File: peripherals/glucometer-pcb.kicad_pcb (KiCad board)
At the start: 2 copper layers, 36.5 x 59.9 mm, 19 parts, among them IC1 RC4558IP, IC2 LM1458N, IC3 RC4558IP

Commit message: change name
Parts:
- removed REF** (x2): MountingHole_2.2mm_M2_ISO7380, MountingHole:MountingHole_2.2mm_M2_ISO7380
- removed TP3: SIGNAL_OUT, TestPoint:TestPoint_Keystone_5015_Micro-Minature
- added BZ1: Buzzer, Buzzer_Beeper:MagneticBuzzer_Kingstate_KCG0601, F.Cu at (120.0, 106.7)
- added D1: LED, LED_THT:LED_D3.0mm_Clear, F.Cu at (121.1, 136.9)
- added D2: LED, LED_THT:LED_D3.0mm_FlatTop, F.Cu at (118.2, 127.7)
- added R3: 120, Resistor_THT:R_Axial_DIN0204_L3.6mm_D1.6mm_P7.62mm_Horizontal, F.Cu at (114.7, 115.1)
- added R4: 240, Resistor_THT:R_Axial_DIN0204_L3.6mm_D1.6mm_P7.62mm_Horizontal, F.Cu at (114.6, 119.1)
- added U1: ESP32_DevKit_V1_DOIT, esp32_devkit_v1_doit:esp32_devkit_v1_doit_own_ESP, F.Cu at (141.1, 111.0)
- moved TP2 76.4 mm to (119.7, 152.4), turned to 0 degrees
- moved TP1 65.2 mm to (119.8, 145.9), turned to 0 degrees
- moved D3 56.7 mm to (134.9, 172.1)
- moved C1 53.5 mm to (138.5, 130.3)
- moved R6 52.6 mm to (125.9, 164.0)
- moved C2 52.2 mm to (130.7, 157.7)
- moved C3 52.2 mm to (138.6, 125.6)
- moved R1 52.0 mm to (152.7, 124.0)
- moved R2 52.0 mm to (152.8, 127.8)
- moved R5 52.0 mm to (141.9, 145.9)
- moved R7 52.0 mm to (146.7, 156.8)
- moved R8 52.0 mm to (146.7, 153.6)
- moved R9 52.0 mm to (149.0, 149.3)
- moved IC1 52.0 mm to (149.8, 136.3)
- moved IC2 52.0 mm to (127.3, 151.8)
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- renumbered D1 to D3, R3 to R5, R4 to R6, R5 to R7, R6 to R8, R7 to R9
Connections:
- net Net-(IC3-Pad6) renamed SIGNAL_OUT
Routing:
- net Net-(BZ1-Pad1): track 0.00 -> 79.1 mm
- net Net-(R3-Pad2): track 0.00 -> 77.4 mm
- net VCC: track 111.8 -> 176.5 mm
- net Net-(D2-Pad1): track 0.00 -> 54.9 mm
- net Net-(D2-Pad2): track 0.00 -> 37.6 mm
- net Net-(D1-Pad2): track 0.00 -> 19.1 mm
- net SIGNAL_OUT: track 84.2 -> 98.8 mm
- net GND: track 101.5 -> 112.7 mm
- net Net-(BZ1-Pad2): track 0.00 -> 9.27 mm
- net /PWD_1.65: track 96.3 -> 102.6 mm
- net Net-(C2-Pad2): track 55.9 -> 50.4 mm
- net Net-(C1-Pad1): track 19.4 -> 23.0 mm
- net /SIGNAL_1: track 69.6 -> 71.2 mm
- net /SIGNAL_2: track 16.4 -> 17.5 mm
- net Net-(C2-Pad1): track 23.0 -> 22.1 mm
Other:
- board outline removed

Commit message: emmiter circuit
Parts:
- removed C1: 10u, Capacitor_THT:CP_Radial_Tantal_D7.0mm_P5.00mm
- removed C2: 15p, Capacitor_THT:CP_Radial_D8.0mm_P3.80mm
- removed C3: 100n, Capacitor_THT:CP_Radial_Tantal_D7.0mm_P5.00mm
- removed D3: D_Photo, LED_SMD:LED_2010_5025Metric
- removed IC1, IC3: RC4558IP, Custom:DIP794W53P254L959H508Q8N
- removed IC2: LM1458N, Custom:MC1458N
- removed the R1 at (152.7, 124.0)
- removed the R2 at (152.8, 127.8)
- removed R5: 25k, Resistor_THT:R_Axial_DIN0204_L3.6mm_D1.6mm_P7.62mm_Horizontal
- removed R6, R9: 100k, Resistor_THT:R_Axial_DIN0204_L3.6mm_D1.6mm_P7.62mm_Horizontal
- removed R7: 330k, Resistor_THT:R_Axial_DIN0204_L3.6mm_D1.6mm_P7.62mm_Horizontal
- removed R8: 1k, Resistor_THT:R_Axial_DIN0204_L3.6mm_D1.6mm_P7.62mm_Horizontal
- removed TP2: TestPoint, TestPoint:TestPoint_Keystone_5015_Micro-Minature
- added 3V3_OUT1: TestPoint, TestPoint:TestPoint_Keystone_5015_Micro-Minature, B.Cu at (195.6, 71.1)
- added BT1: Battery_Cell, Connector_Wire:SolderWire-0.1sqmm_1x02_P3.6mm_D0.4mm_OD1mm, F.Cu at (226.1, 71.1)
- added R3: 120, Resistor_THT:R_Axial_DIN0204_L3.6mm_D1.6mm_P7.62mm_Horizontal, F.Cu at (226.8, 106.8)
- D2: renamed from D1; value LED -> EMITTER
- R2: renamed from R4; value 240 -> 120
- TP1: moved to B.Cu
- U1: footprint esp32_devkit_v1_doit:esp32_devkit_v1_doit_own_ESP -> esp32_devkit_v1_doit:esp32_devkit_v1_doit
- moved R2 113.2 mm to (214.6, 66.0)
- moved TP1 112.0 mm to (203.2, 71.1), turned to 180 degrees
- moved D1 111.2 mm to (213.9, 71.1), turned to 180 degrees
- moved D2 89.8 mm to (210.8, 132.1)
- moved R1 77.9 mm to (188.7, 90.8), turned to 90 degrees
- moved BZ1 69.1 mm to (188.8, 99.7), turned to 90 degrees
- moved U1 67.7 mm to (208.3, 119.4)
- renumbered D2 to D1, R3 to R1
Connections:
- D1 pad 1: Net-(D2-Pad1) -> Net-(D1-Pad1)
- D1 pad 2: Net-(D2-Pad2) -> Net-(D1-Pad2)
- D2 pad 1: VCC -> Net-(D2-Pad1)
- D2 pad 2: Net-(D1-Pad2) -> Net-(D2-Pad2)
- R1 pad 2: Net-(R3-Pad2) -> GND
- R2 pad 1: Net-(D1-Pad2) -> Net-(D1-Pad1)
- R2 pad 2: Net-(D2-Pad1) -> GND
- TP1 pad 1: GND -> SIGNAL_OUT
- U1 pad 1: VCC -> unconnected-(U1-Pad1)
- U1 pad 11: unconnected-(U1-Pad11) -> Net-(D1-Pad2)
- U1 pad 14: unconnected-(U1-Pad14) -> GND
- U1 pad 15: unconnected-(U1-Pad15) -> Net-(BT1-Pad1)
- U1 pad 16: unconnected-(U1-Pad16) -> VCC
- U1 pad 17: Net-(D2-Pad1) -> GND
- U1 pad 18: unconnected-(U1-Pad18) -> Net-(D2-Pad2)
- U1 pad 19: unconnected-(U1-Pad19) -> Net-(BZ1-Pad1)
- U1 pad 2: Net-(R3-Pad2) -> unconnected-(U1-Pad2)
- U1 pad 23: Net-(D2-Pad2) -> unconnected-(U1-Pad23)
- U1 pad 4: Net-(BZ1-Pad1) -> unconnected-(U1-Pad4)
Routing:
- net VCC: track 176.5 -> 12.7 mm
- net /PWD_1.65: track 102.6 -> 0.00 mm
- net Net-(R3-Pad2): track 77.4 -> 0.00 mm
- net /SIGNAL_1: track 71.2 -> 0.00 mm
- net Net-(BZ1-Pad1): track 79.1 -> 12.2 mm
- net GND: track 112.7 -> 46.6 mm
- net SIGNAL_OUT: track 98.8 -> 42.5 mm
- net Net-(C2-Pad2): track 50.4 -> 0.00 mm
- net Net-(IC3-Pad7): track 50.0 -> 0.00 mm
- net Net-(C1-Pad1): track 23.0 -> 0.00 mm
- net Net-(C2-Pad1): track 22.1 -> 0.00 mm
- net Net-(D2-Pad1): track 54.9 -> 33.7 mm
- net /SIGNAL_2: track 17.5 -> 0.00 mm
- net Net-(IC1-Pad3): track 15.6 -> 0.00 mm
- net Net-(BT1-Pad1): track 0.00 -> 14.8 mm
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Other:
- board outline added: 46.1 x 72.7 mm

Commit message: fixed PCB
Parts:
- added INTERRUPT_GPIO18: SW_Push, Connector_Wire:SolderWire-0.1sqmm_1x02_P3.6mm_D0.4mm_OD1mm, F.Cu at (190.7, 70.6)
- moved R1 12.8 mm to (216.8, 78.7), turned to -90 degrees
- moved R2 11.9 mm to (216.8, 100.3)
- moved SIGNAL_IN1 6.83 mm to (210.0, 70.7)
- moved Testigo1 6.28 mm to (220.2, 70.4)
- moved R3 5.24 mm to (191.7, 86.5)
- moved 3V3_OUT1 5.10 mm to (200.7, 70.7)
- moved BZ1 4.47 mm to (189.8, 95.4)
- moved BATTERY1 3.10 mm to (229.1, 70.8)
- renumbered BT1 to BATTERY1, R2 to R1, R3 to R2, R1 to R3, TP1 to SIGNAL_IN1, D1 to Testigo1
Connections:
- BZ1 pad 1: Net-(BZ1-Pad1) -> Net-(U1-Pad24)
- D2 pad 2: Net-(D2-Pad2) -> Net-(U1-Pad30)
- SIGNAL_IN1 pad 1: SIGNAL_OUT -> Net-(SIGNAL_IN1-Pad1)
- Testigo1 pad 2: Net-(D1-Pad2) -> Net-(U1-Pad29)
- U1 pad 11: Net-(D1-Pad2) -> unconnected-(U1-Pad11)
- U1 pad 18: Net-(D2-Pad2) -> unconnected-(U1-Pad18)
- U1 pad 19: Net-(BZ1-Pad1) -> unconnected-(U1-Pad19)
- U1 pad 24: unconnected-(U1-Pad24) -> Net-(U1-Pad24)
- U1 pad 25: unconnected-(U1-Pad25) -> Net-(U1-Pad25)
- U1 pad 26: unconnected-(U1-Pad26) -> Net-(SIGNAL_IN1-Pad1)
- U1 pad 29: unconnected-(U1-Pad29) -> Net-(U1-Pad29)
- U1 pad 30: unconnected-(U1-Pad30) -> Net-(U1-Pad30)
- U1 pad 8: SIGNAL_OUT -> unconnected-(U1-Pad8)
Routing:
- net Net-(U1-Pad29): track 0.00 -> 56.5 mm
- net Net-(D2-Pad2): track 48.4 -> 0.00 mm
- net Net-(SIGNAL_IN1-Pad1): track 0.00 -> 46.3 mm
- net SIGNAL_OUT: track 42.5 -> 0.00 mm
- net Net-(U1-Pad25): track 0.00 -> 42.3 mm
- net Net-(D1-Pad2): track 26.8 -> 0.00 mm
- net Net-(U1-Pad30): track 0.00 -> 22.8 mm
- net Net-(BZ1-Pad1): track 12.2 -> 0.00 mm
- net Net-(U1-Pad24): track 0.00 -> 11.2 mm
- net Net-(Testigo1-Pad1): track 5.38 -> 9.27 mm
- net Net-(BZ1-Pad2): track 5.80 -> 8.35 mm
- net VCC: track 12.7 -> 15.2 mm
- net GND: track 46.6 -> 48.4 mm
- net Net-(BATTERY1-Pad1): track 14.8 -> 16.4 mm
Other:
- board size 46.1 x 72.7 mm -> 46.3 x 68 mm

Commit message: changes
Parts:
- added OLED_PINS1: Conn_01x04_Female, Connector_Wire:SolderWire-0.1sqmm_1x04_P3.6mm_D0.4mm_OD1mm, B.Cu at (213.8, 111.8)
- moved BATTERY1 13.2 mm to (215.9, 70.8), turned to 0 degrees
- moved R2 8.54 mm to (225.3, 78.6)
- moved Testigo1 4.65 mm to (224.8, 71.0), turned to 0 degrees
- moved D1 1.12 mm to (209.7, 132.1)
- moved R3 0.97 mm to (217.7, 100.2)
- renumbered D2 to D1, INTERRUPT_GPIO18 to INTERRUPT_GPIO1, R3 to R1, R1 to R2, R2 to R3
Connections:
- Testigo1 pad 2: Net-(U1-Pad29) -> Net-(U1-Pad8)
- U1 pad 21: unconnected-(U1-Pad21) -> Net-(SIGNAL_IN1-Pad1)
- U1 pad 26: Net-(SIGNAL_IN1-Pad1) -> Net-(OLED_PINS1-Pad3)
- U1 pad 29: Net-(U1-Pad29) -> Net-(OLED_PINS1-Pad4)
- U1 pad 8: unconnected-(U1-Pad8) -> Net-(U1-Pad8)
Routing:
- net Net-(U1-Pad29): track 56.5 -> 0.00 mm
- net unconnected-(U1-Pad22): track 0.00 -> 28.9 mm
- net Net-(BATTERY1-Pad1): track 16.4 -> 0.00 mm
- net Net-(SIGNAL_IN1-Pad1): track 46.3 -> 32.5 mm
- net Net-(OLED_PINS1-Pad3): track 0.00 -> 12.1 mm
- net Net-(OLED_PINS1-Pad4): track 0.00 -> 11.1 mm
- net Net-(R2-Pad1): track 9.27 -> 0.00 mm
- net GND: track 48.4 -> 51.9 mm
- net Net-(D1-Pad1): track 34.2 -> 35.4 mm

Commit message: last update emmiter pcb
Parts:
- removed R2: 120, Resistor_THT:R_Axial_DIN0204_L3.6mm_D1.6mm_P7.62mm_Horizontal
- removed Testigo1: LED, LED_THT:LED_D3.0mm_FlatTop
- added REF**: MountingHole_2.2mm_M2, MountingHole:MountingHole_2.2mm_M2, F.Cu at (185.7, 131.0)
- added REF**: MountingHole_2.2mm_M2, MountingHole:MountingHole_2.2mm_M2, F.Cu at (223.9, 130.7)
- added REF**: MountingHole_2.2mm_M2, MountingHole:MountingHole_2.2mm_M2, F.Cu at (185.7, 70.6)
- added REF**: MountingHole_2.2mm_M2, MountingHole:MountingHole_2.2mm_M2, F.Cu at (223.9, 70.9)
- moved R3 19.2 mm to (216.9, 119.4), turned to 180 degrees
- moved BATTERY1 3.72 mm to (219.6, 70.9), turned to 180 degrees
- moved OLED_PINS1 1.27 mm to (212.6, 111.8)
- moved R1 1.11 mm to (191.7, 87.6)
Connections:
- net VCC renamed Net-(3V3_OUT1-Pad1)
- U1 pad 21: Net-(SIGNAL_IN1-Pad1) -> unconnected-(U1-Pad21)
- U1 pad 8: Net-(U1-Pad8) -> unconnected-(U1-Pad8)
- U1 pad 9: unconnected-(U1-Pad9) -> Net-(SIGNAL_IN1-Pad1)
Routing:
- net GND: track 51.9 -> 0.09 mm
- net Net-(3V3_OUT1-Pad1): track 15.2 -> 47.6 mm
- net unconnected-(U1-Pad22): track 28.9 -> 0.00 mm
- net Net-(D1-Pad1): track 35.4 -> 15.7 mm
- net Net-(BATTERY1-Pad1): track 0.00 -> 13.5 mm
- net Net-(OLED_PINS1-Pad4): track 11.1 -> 20.4 mm
- net Net-(OLED_PINS1-Pad3): track 12.1 -> 17.8 mm
- net Net-(BZ1-Pad2): track 8.35 -> 7.00 mm
- added copper zone on B.Cu, net GND
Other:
- board size 46.3 x 68 mm -> 43.9 x 66.9 mm

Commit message: last update
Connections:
- SIGNAL_IN1 pad 1: Net-(SIGNAL_IN1-Pad1) -> Net-(U1-Pad4)
- U1 pad 4: unconnected-(U1-Pad4) -> Net-(U1-Pad4)
- U1 pad 9: Net-(SIGNAL_IN1-Pad1) -> unconnected-(U1-Pad9)
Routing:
- net Net-(U1-Pad4): track 0.00 -> 45.8 mm
- net Net-(SIGNAL_IN1-Pad1): track 32.9 -> 0.00 mm
- removed copper zone on B.Cu, net GND
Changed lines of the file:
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@@
   (net 8 "unconnected-(U1-Pad10)")
   (net 9 "unconnected-(U1-Pad12)")
-  (net 10 "unconnected-(U1-Pad13)")
-  (net 11 "unconnected-(U1-Pad20)")
-  (net 12 "Net-(SIGNAL_IN1-Pad1)")
+  (net 10 "Net-(U1-Pad4)")
+  (net 11 "unconnected-(U1-Pad9)")
+  (net 12 "unconnected-(U1-Pad20)")
   (net 13 "unconnected-(U1-Pad11)")
   (net 14 "unconnected-(U1-Pad19)")
@@
   (net 18 "unconnected-(U1-Pad1)")
   (net 19 "unconnected-(U1-Pad2)")
-  (net 20 "unconnected-(U1-Pad4)")
+  (net 20 "unconnected-(U1-Pad13)")
   (net 21 "unconnected-(U1-Pad23)")
   (net 22 "unconnected-(U1-Pad18)")
@@
       (net 4 "unconnected-(U1-Pad3)") (pinfunction "SENSOR_VN") (pintype "input+no_connect"))
     (pad "4" thru_hole circle (at -12.7 7.62 180) (size 1.524 1.524) (drill 0.762) (layers *.Cu *.Mask)
-      (net 20 "unconnected-(U1-Pad4)") (pinfunction "IO34") (pintype "input+no_connect"))
+      (net 10 "Net-(U1-Pad4)") (pinfunction "IO34") (pintype "input"))
     (pad "5" thru_hole circle (at -12.7 10.16 180) (size 1.524 1.524) (drill 0.762) (layers *.Cu *.Mask)
       (net 5 "unconnected-(U1-Pad5)") (pinfunction "IO35") (pintype "input+no_connect"))
@@
       (net 31 "unconnected-(U1-Pad8)") (pinfunction "IO25") (pintype "bidirectional+no_connect"))
     (pad "9" thru_hole circle (at -12.7 20.32 180) (size 1.524 1.524) (drill 0.762) (layers *.Cu *.Mask)
-      (net 12 "Net-(SIGNAL_IN1-Pad1)") (pinfunction "IO26") (pintype "bidirectional"))
+      (net 11 "unconnected-(U1-Pad9)") (pinfunction "IO26") (pintype "bidirectional+no_connect"))
     (pad "10" thru_hole circle (at -12.7 22.86 180) (size 1.524 1.524) (drill 0.762) (layers *.Cu *.Mask)
       (net 8 "unconnected-(U1-Pad10)") (pinfunction "IO27") (pintype "bidirectional+no_connect"))
@@
       (net 9 "unconnected-(U1-Pad12)") (pinfunction "IO12") (pintype "bidirectional+no_connect"))
     (pad "13" thru_hole circle (at -12.7 30.48 180) (size 1.524 1.524) (drill 0.762) (layers *.Cu *.Mask)
-      (net 10 "unconnected-(U1-Pad13)") (pinfunction "IO13") (pintype "bidirectional+no_connect"))
+      (net 20 "unconnected-(U1-Pad13)") (pinfunction "IO13") (pintype "bidirectional+no_connect"))
     (pad "14" thru_hole circle (at -12.7 33.02 180) (size 1.524 1.524) (drill 0.762) (layers *.Cu *.Mask)
       (net 17 "GND") (pinfunction "GND") (pintype "power_in"))
@@
       (net 14 "unconnected-(U1-Pad19)") (pinfunction "IO2") (pintype "bidirectional+no_connect"))
     (pad "20" thru_hole circle (at 12.7 25.4 180) (size 1.524 1.524) (drill 0.762) (layers *.Cu *.Mask)
-      (net 11 "unconnected-(U1-Pad20)") (pinfunction "IO4") (pintype "bidirectional+no_connect"))
+      (net 12 "unconnected-(U1-Pad20)") (pinfunction "IO4") (pintype "bidirectional+no_connect"))
     (pad "21" thru_hole circle (at 12.7 22.86 180) (size 1.524 1.524) (drill 0.762) (layers *.Cu *.Mask)
       (net 25 "unconnected-(U1-Pad21)") (pinfunction "IO16") (pintype "bidirectional+no_connect"))
@@
     (fp_line (start 1.35 0.5) (end -1.35 0.5) (layer "B.Fab") (width 0.15))
     (pad "1" smd rect (at 0 0 180) (size 3.4 1.8) (layers "B.Cu" "B.Paste" "B.Mask")
-      (net 12 "Net-(SIGNAL_IN1-Pad1)") (pinfunction "1") (pintype "passive"))
+      (net 10 "Net-(U1-Pad4)") (pinfunction "1") (pintype "passive"))
     (model "${KICAD6_3DMODEL_DIR}/TestPoint.3dshapes/TestPoint_Keystone_5015_Micro-Minature.wrl"
       (offset (xyz 0 0 0))
@@
   (segment (start 189.772519 98.332519) (end 195.58 104.14) (width 0.3) (layer "B.Cu") (net 3))
   (segment (start 189.772519 95.391372) (end 189.772519 98.332519) (width 0.3) (layer "B.Cu") (net 3))
-  (segment (start 210.017152 70.693906) (end 210.017152 88.097152) (width 0.3) (layer "B.Cu") (net 12))
-  (segment (start 210.017152 88.097152) (end 220.98 99.06) (width 0.3) (layer "B.Cu") (net 12))
+  (segment (start 210.017152 70.693906) (end 209.798438 70.91262) (width 0.3) (layer "B.Cu") (net 10))
+  (segment (start 209.798438 70.91262) (end 209.798438 100.578438) (width 0.3) (layer "B.Cu") (net 10))
+  (segment (start 209.798438 100.578438) (end 220.98 111.76) (width 0.3) (layer "B.Cu") (net 10))
   (segment (start 202.474129 111.749481) (end 202.411893 111.811717) (width 0.3) (layer "B.Cu") (net 17))
   (segment (start 209.700449 132.123846) (end 216.923703 124.900592) (width 0.3) (layer "B.Cu") (net 23))
@@
   (segment (start 219.617832 70.85264) (end 220.98 72.214808) (width 0.3) (layer "B.Cu") (net 30))
   (segment (start 220.98 72.214808) (end 220.98 83.82) (width 0.3) (layer "B.Cu") (net 30))
-  (zone (net 17) (net_name "GND") (layer "B.Cu") (hatch edge 0.508)
-    (connect_pads (clearance 0.508))
-    (min_thickness 0.254) (filled_areas_thickness no)
-    (fill yes (thermal_gap 0.508) (thermal_bridge_width 0.508))
-    (polygon
-      (pts
-        (xy 226.761552 67.628281)
-        (xy 226.748296 134.454808)
-        (xy 182.916709 134.429385)
-        (xy 182.903112 134.38905)
-        (xy 182.935063 67.607207)
-      )
-    )
-  )
 )

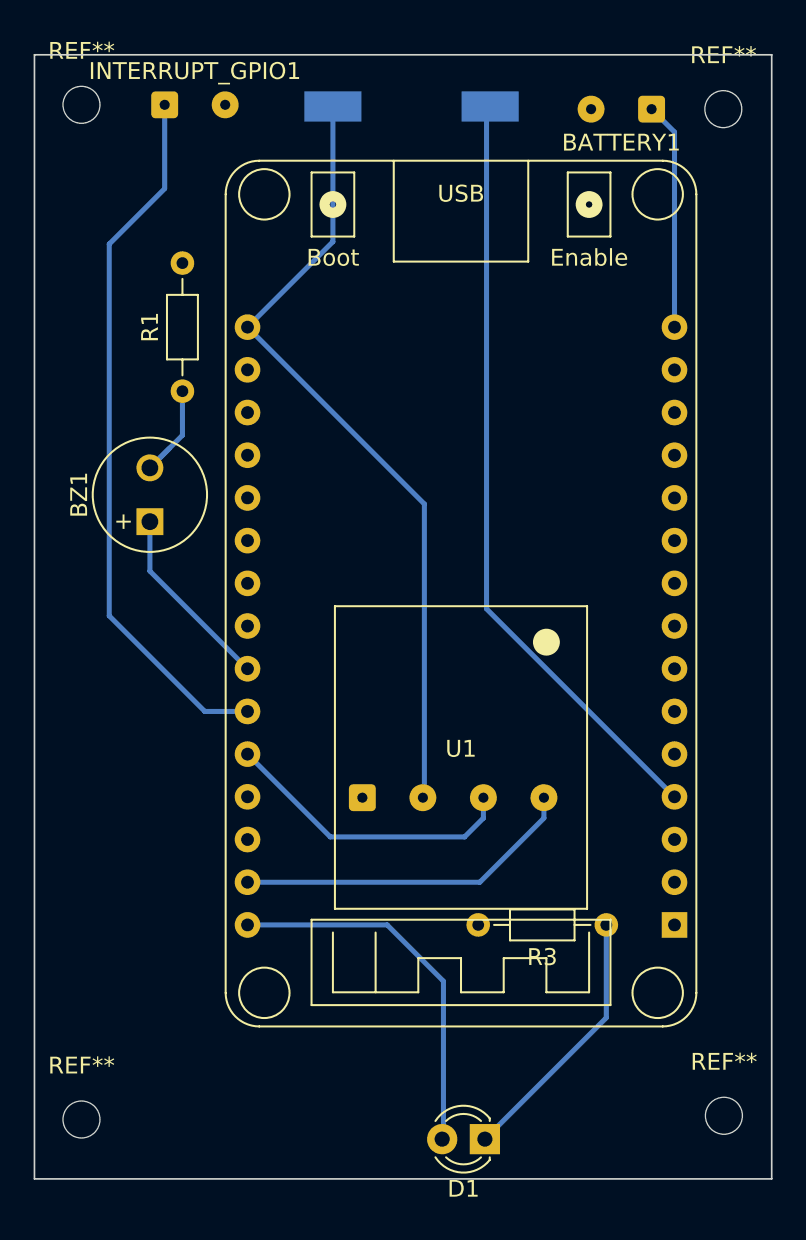
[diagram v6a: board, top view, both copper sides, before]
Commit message: updated footprints
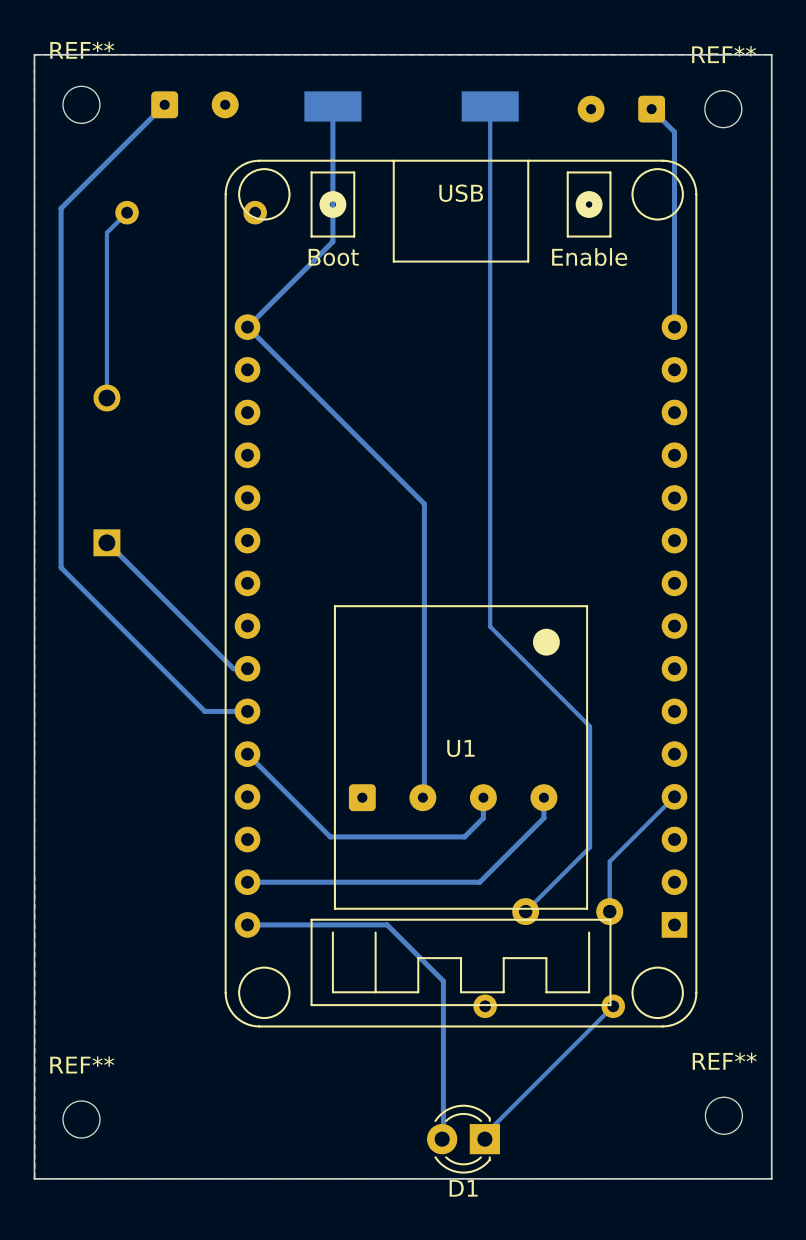
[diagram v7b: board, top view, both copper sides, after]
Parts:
- added 100nF1: CAP, Capacitor_THT:C_Disc_D4.3mm_W1.9mm_P5.00mm, B.Cu at (212.1, 118.6)
- BATTERY1, INTERRUPT_GPIO1, R1: moved to B.Cu
- BZ1: footprint Buzzer_Beeper:MagneticBuzzer_Kingstate_KCG0601 -> Buzzer_Beeper:MagneticBuzzer_ProSignal_ABI-009-RC; moved to B.Cu
- R2: renamed from R3; moved to B.Cu
- moved R1 11.1 mm to (188.4, 77.0), turned to 0 degrees
- moved R2 4.86 mm to (217.3, 124.2)
- moved BZ1 2.69 mm to (187.2, 96.2)
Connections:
- SIGNAL_IN1 pad 1: Net-(U1-Pad4) -> Net-(100nF1-Pad1)
- U1 pad 4: Net-(U1-Pad4) -> Net-(100nF1-Pad2)
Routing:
- net Net-(100nF1-Pad1): track 0.00 -> 52.2 mm
- net Net-(U1-Pad4): track 45.8 -> 0.00 mm
- net Net-(100nF1-Pad2): track 0.00 -> 8.70 mm
- net Net-(D1-Pad1): track 15.7 -> 11.1 mm
- net Net-(BZ1-Pad2): track 7.00 -> 11.5 mm
- net Net-(INTERRUPT_GPIO1-Pad1): track 42.3 -> 44.7 mm
- added copper zone on B.Cu, net GND

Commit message: updated pcbs
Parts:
- moved REF** 171.2 mm to (21.5, 82.5)
- moved REF** 171.2 mm to (21.4, 22.5)
- moved INTERRUPT_GPIO1 169.8 mm to (27.9, 22.2)
- moved R1 169.8 mm to (25.7, 28.6)
- moved SIGNAL_IN1 169.8 mm to (47.3, 22.3)
- moved 100nF1 169.8 mm to (49.4, 70.1)
- moved 3V3_OUT1 169.8 mm to (37.9, 22.3)
- moved BATTERY1 169.8 mm to (56.9, 22.4)
- moved BZ1 169.8 mm to (24.5, 47.8)
- moved D1 169.8 mm to (47.0, 83.7)
- moved OLED_PINS1 169.8 mm to (49.8, 63.4)
- moved R2 169.8 mm to (54.6, 75.8)
- moved U1 169.8 mm to (45.5, 70.9)
- moved REF** 161.6 mm to (69.7, 82.5)
- moved REF** 161.5 mm to (69.8, 22.4)
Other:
- board size 43.9 x 66.9 mm -> 54.8 x 66.9 mm
